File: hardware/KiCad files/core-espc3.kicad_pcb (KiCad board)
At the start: 2 copper layers, 88 x 17.1 mm, 16 parts, among them J2 Conn_01x04_Pin, U3 TMAG5273A1QDBVR, U4 TMR1208S, U5 THVD1406DR

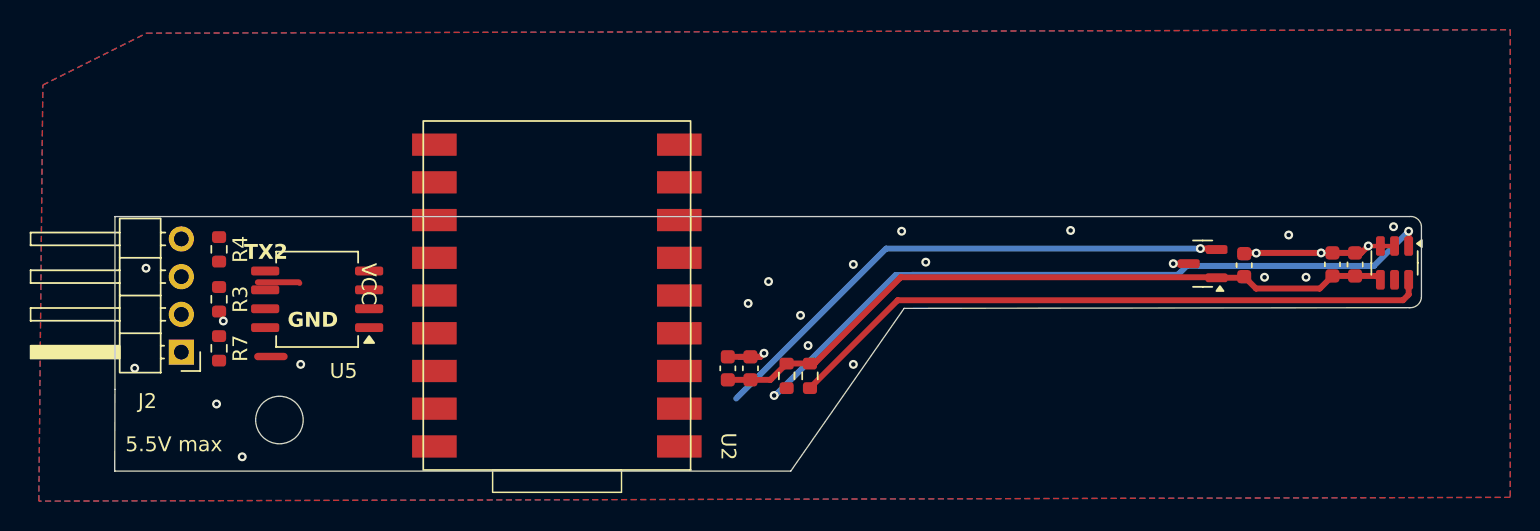
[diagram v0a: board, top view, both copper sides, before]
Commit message: Initial PCB Routing Add I2C "expansion" connector for AHT20 + BMP280 sensor
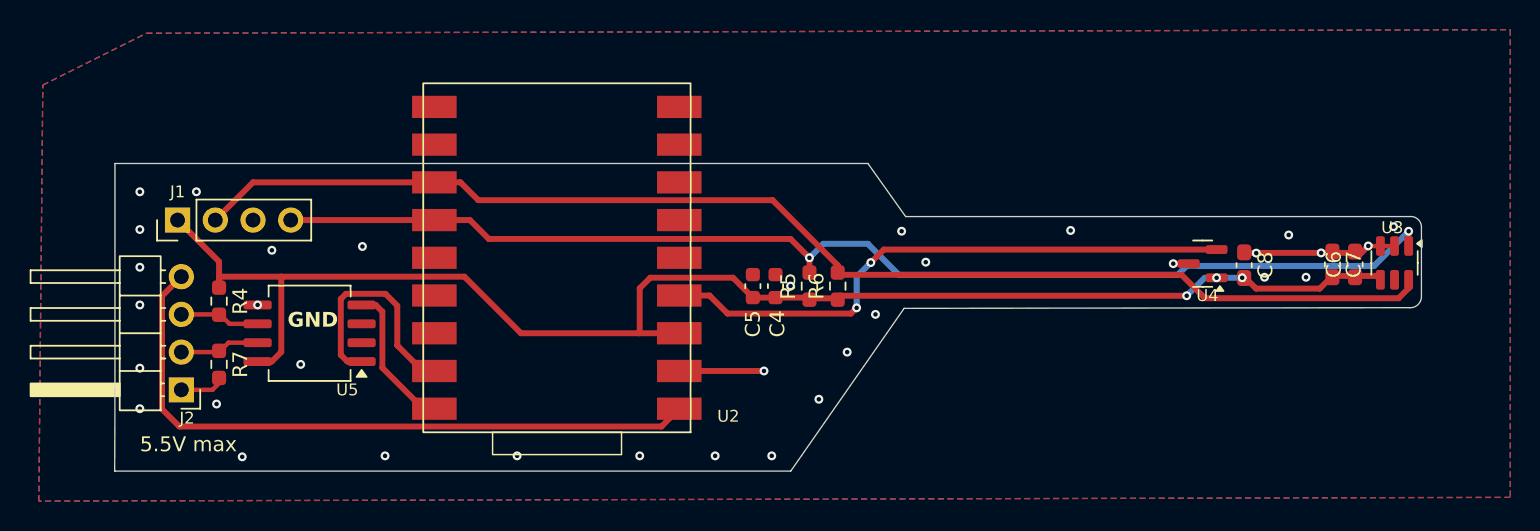
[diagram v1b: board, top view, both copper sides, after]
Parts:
- removed R3: 120, Resistor_SMD:R_0603_1608Metric
- removed REF**: MountingHole_3.2mm_M3, MountingHole:MountingHole_3.2mm_M3
- added J1: Conn_01x04_Pin, Connector_PinHeader_2.54mm:PinHeader_1x04_P2.54mm_Vertical, F.Cu at (104.1, 86.4)
- C6, C7, C8: footprint Capacitor_SMD:C_0603_1608Metric -> Capacitor_SMD:C_0603_1608Metric_Pad1.08x0.95mm_HandSolder
- R4, R5, R6, R7: footprint Resistor_SMD:R_0603_1608Metric -> Resistor_SMD:R_0603_1608Metric_Pad0.98x0.95mm_HandSolder
- moved R6 6.33 mm to (148.6, 90.8), turned to 90 degrees
- moved R5 6.24 mm to (146.7, 90.8), turned to 90 degrees
- moved C4 5.79 mm to (144.4, 90.8)
- moved C5 5.79 mm to (142.9, 90.8)
- moved R4 3.49 mm to (106.9, 91.8)
- moved J2 2.54 mm to (104.4, 97.8)
- moved U2 2.54 mm to (130.2, 89.2)
- moved U5 2.34 mm to (113.0, 94.0)
- moved R7 1.08 mm to (106.9, 96.1)
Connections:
- net A4 renamed D4
- net A5 renamed D5
- net A6 renamed D6
- U2 pad 11: SPEED -> D7
- U2 pad 4: A0 -> SPEED
- U5 pad 1: unconnected-(U5-R-Pad1) -> TX
- U5 pad 4: unconnected-(U5-D-Pad4) -> RX
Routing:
- net +3.3V: track 47.7 -> 101.3 mm, vias 0 -> 3
- net +5V: track 0.00 -> 45.3 mm
- net SDA: track 43.9 -> 85.8 mm
- net SCL: track 48.3 -> 80.9 mm
- net TX: track 0.00 -> 15.5 mm
- net RX: track 0.00 -> 10.0 mm
- net /B: track 0.00 -> 5.40 mm
- net GND: track 15.9 -> 20.4 mm, vias 24 -> 34
- net SPEED: track 36.6 -> 39.7 mm, vias 1 -> 2
- net /A: track 2.85 -> 5.45 mm
- net (no net): track 1.77 -> 0.00 mm
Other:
- board size 88 x 17.1 mm -> 88 x 20.7 mm
- board text removed: "TX2"
- board text removed: "VCC"
